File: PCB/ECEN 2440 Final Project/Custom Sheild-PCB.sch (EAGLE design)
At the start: 9 parts

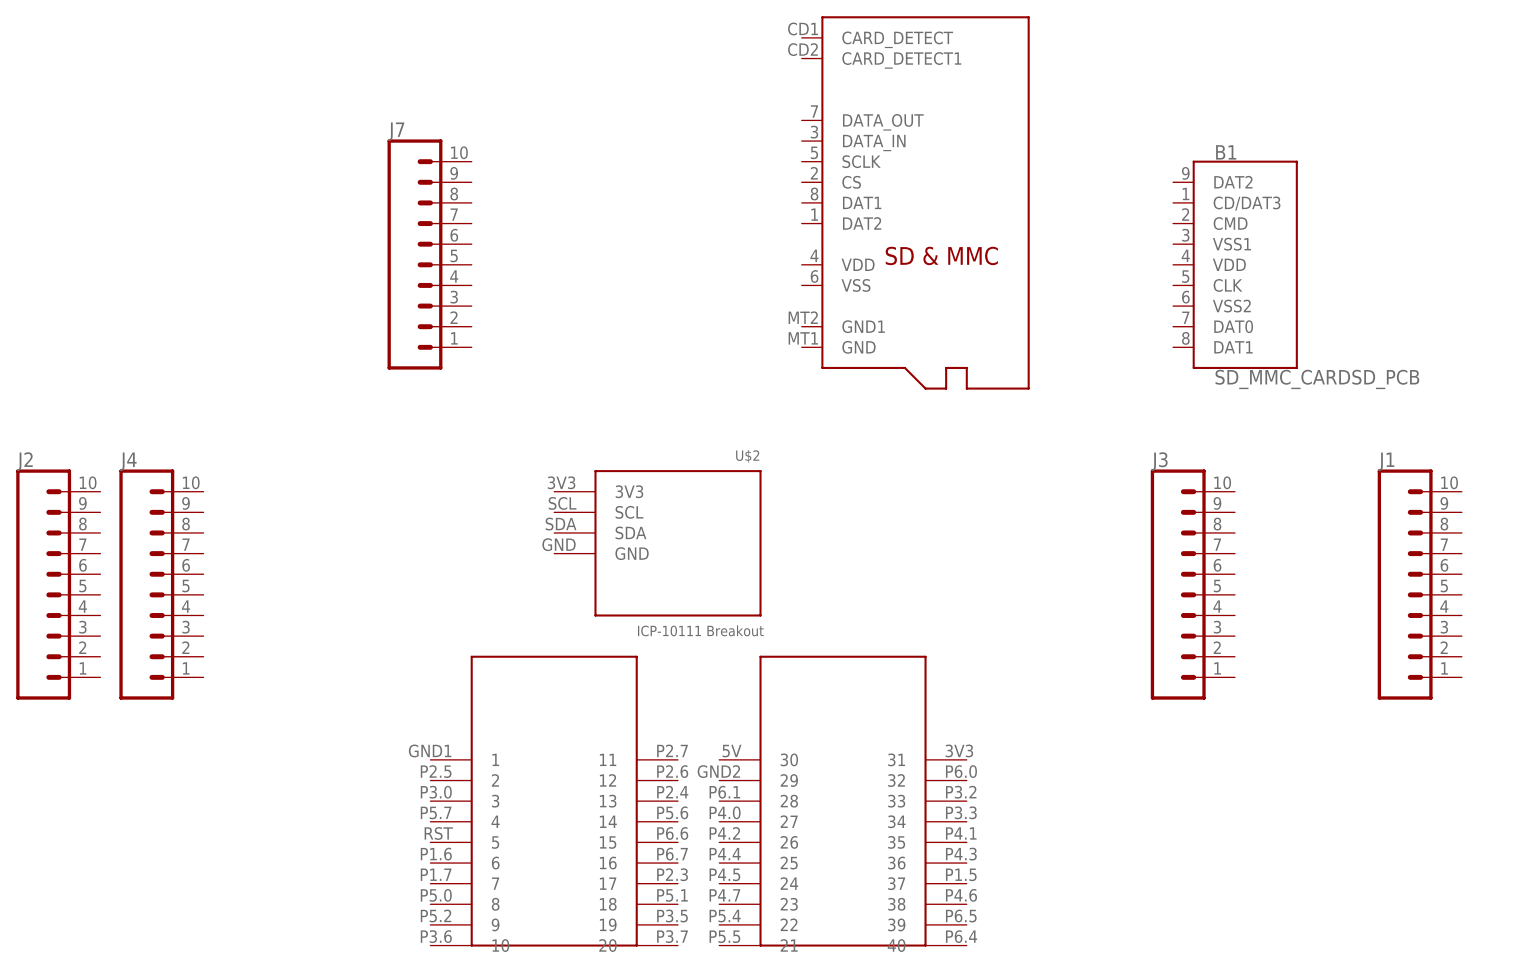
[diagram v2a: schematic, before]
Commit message: Added the radio device, and made a couple connections
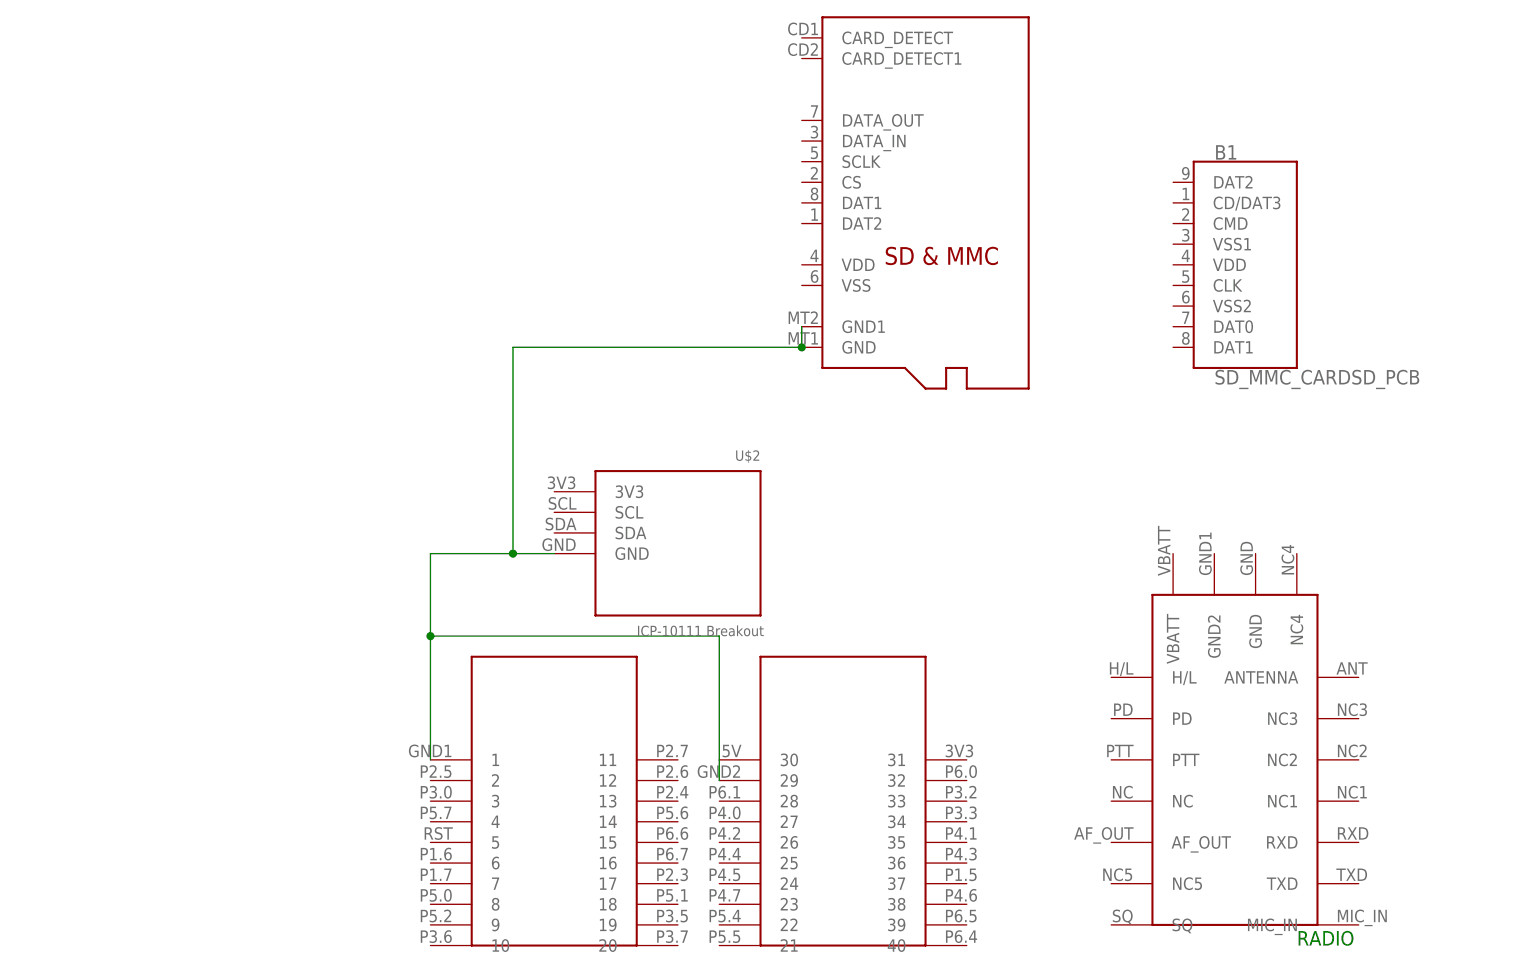
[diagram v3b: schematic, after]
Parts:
- removed J1, J2, J3, J4, J7: (no value), SparkFun-Connectors:CONN_10"
- added U$4: RADIO, Custom Library:RADIO
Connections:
- new net GND1: U$1.GND, U$1.GND1, U$2.GND, U$3.1, U$3.29
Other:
- note added: "RADIO"
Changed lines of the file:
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@@
 </classes>
 <parts>
-<part name="J1" library="SparkFun-Connectors" library_urn="urn:adsk.eagle:library:513" deviceset="CONN_10" device="&quot;" package3d_urn="urn:adsk.eagle:package:38157/1"/>
-<part name="J2" library="SparkFun-Connectors" library_urn="urn:adsk.eagle:library:513" deviceset="CONN_10" device="&quot;" package3d_urn="urn:adsk.eagle:package:38157/1"/>
-<part name="J3" library="SparkFun-Connectors" library_urn="urn:adsk.eagle:library:513" deviceset="CONN_10" device="&quot;" package3d_urn="urn:adsk.eagle:package:38157/1"/>
-<part name="J4" library="SparkFun-Connectors" library_urn="urn:adsk.eagle:library:513" deviceset="CONN_10" device="&quot;" package3d_urn="urn:adsk.eagle:package:38157/1"/>
-<part name="J7" library="SparkFun-Connectors" library_urn="urn:adsk.eagle:library:513" deviceset="CONN_10" device="&quot;" package3d_urn="urn:adsk.eagle:package:38157/1"/>
 <part name="B1" library="SparkFun-Boards" library_urn="urn:adsk.eagle:library:509" deviceset="SD_MMC_CARD" device="SD_PCB" package3d_urn="urn:adsk.eagle:package:37313/1"/>
 <part name="U$1" library="adafruit" library_urn="urn:adsk.eagle:library:420" deviceset="MICROSD" device="" package3d_urn="urn:adsk.eagle:package:6240723/1"/>
 <part name="U$2" library="Custom Library" deviceset="ALTIMETER" device=""/>
 <part name="U$3" library="Custom Library" deviceset="MSP432" device=""/>
+<part name="U$4" library="Custom Library" deviceset="RADIO" device=""/>
 </parts>
 <sheets>
 <sheet>
 <plain>
+<text x="142.24" y="0" size="1.778" layer="91">RADIO</text>
 </plain>
 <instances>
-<instance part="J1" gate="G$1" x="152.4" y="50.8" smashed="yes">
-<attribute name="VALUE" x="152.4" y="28.194" size="1.778" layer="96" font="vector"/>
-<attribute name="NAME" x="152.4" y="58.928" size="1.778" layer="95" font="vector"/>
-</instance>
-<instance part="J2" gate="G$1" x="-15.24" y="50.8" smashed="yes">
-<attribute name="VALUE" x="-15.24" y="28.194" size="1.778" layer="96" font="vector"/>
-<attribute name="NAME" x="-15.24" y="58.928" size="1.778" layer="95" font="vector"/>
-</instance>
-<instance part="J3" gate="G$1" x="124.46" y="50.8" smashed="yes">
-<attribute name="VALUE" x="124.46" y="28.194" size="1.778" layer="96" font="vector"/>
-<attribute name="NAME" x="124.46" y="58.928" size="1.778" layer="95" font="vector"/>
-</instance>
-<instance part="J4" gate="G$1" x="-2.54" y="50.8" smashed="yes">
-<attribute name="VALUE" x="-2.54" y="28.194" size="1.778" layer="96" font="vector"/>
-<attribute name="NAME" x="-2.54" y="58.928" size="1.778" layer="95" font="vector"/>
-</instance>
-<instance part="J7" gate="G$1" x="30.48" y="91.44" smashed="yes">
-<attribute name="VALUE" x="30.48" y="68.834" size="1.778" layer="96" font="vector"/>
-<attribute name="NAME" x="30.48" y="99.568" size="1.778" layer="95" font="vector"/>
-</instance>
 <instance part="B1" gate="G$1" x="137.16" y="83.82" smashed="yes">
 <attribute name="NAME" x="132.08" y="96.774" size="1.778" layer="95" font="vector"/>
@@
 </instance>
 <instance part="U$3" gate="MSP432" x="50.8" y="27.94" smashed="yes"/>
+<instance part="U$4" gate="G$1" x="124.46" y="2.54" smashed="yes"/>
 </instances>
 <busses>
 </busses>
 <nets>
+<net name="GND1" class="0">
+<segment>
+<pinref part="U$1" gate="G$1" pin="GND1"/>
+<pinref part="U$1" gate="G$1" pin="GND"/>
+<wire x1="81.28" y1="76.2" x2="81.28" y2="73.66" width="0.1524" layer="91"/>
+<pinref part="U$3" gate="MSP432" pin="1"/>
+<pinref part="U$2" gate="G$1" pin="GND"/>
+<wire x1="35.56" y1="22.86" x2="35.56" y2="38.1" width="0.1524" layer="91"/>
+<wire x1="35.56" y1="38.1" x2="35.56" y2="48.26" width="0.1524" layer="91"/>
+<wire x1="35.56" y1="48.26" x2="45.72" y2="48.26" width="0.1524" layer="91"/>
+<pinref part="U$3" gate="MSP432" pin="29"/>
+<wire x1="45.72" y1="48.26" x2="50.8" y2="48.26" width="0.1524" layer="91"/>
+<wire x1="71.12" y1="20.32" x2="71.12" y2="38.1" width="0.1524" layer="91"/>
+<wire x1="71.12" y1="38.1" x2="35.56" y2="38.1" width="0.1524" layer="91"/>
+<junction x="35.56" y="38.1"/>
+<wire x1="81.28" y1="73.66" x2="45.72" y2="73.66" width="0.1524" layer="91"/>
+<wire x1="45.72" y1="73.66" x2="45.72" y2="48.26" width="0.1524" layer="91"/>
+<junction x="81.28" y="73.66"/>
+<junction x="45.72" y="48.26"/>
+</segment>
+</net>
 </nets>
 </sheet>
